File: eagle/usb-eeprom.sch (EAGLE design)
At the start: 3 parts

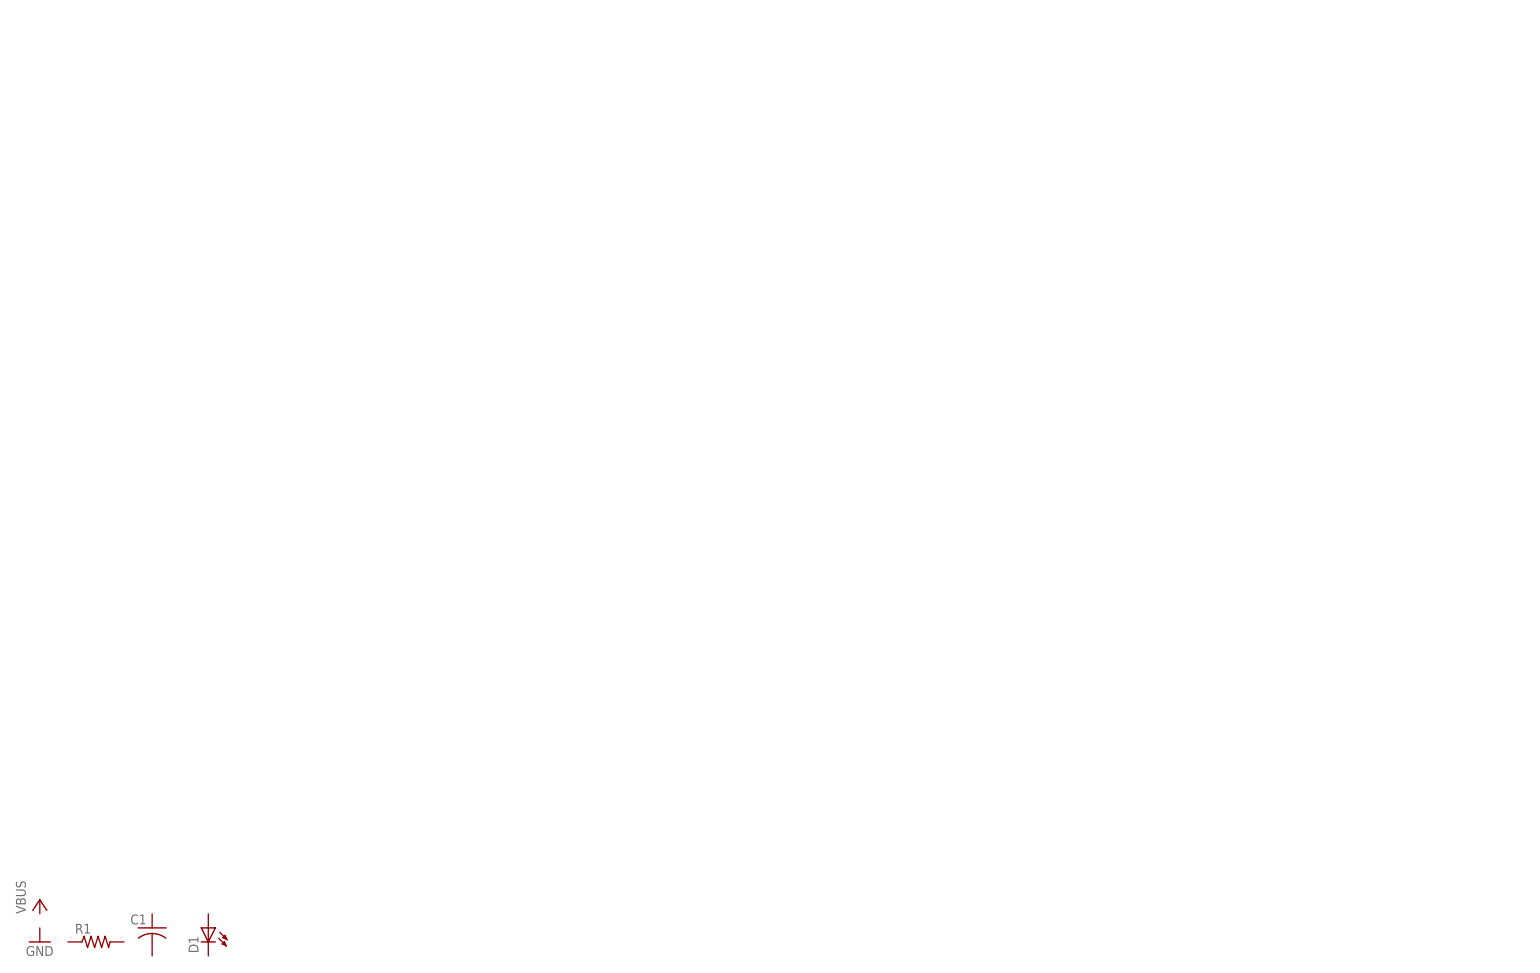
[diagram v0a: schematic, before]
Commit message: Update schematic; generate BOM
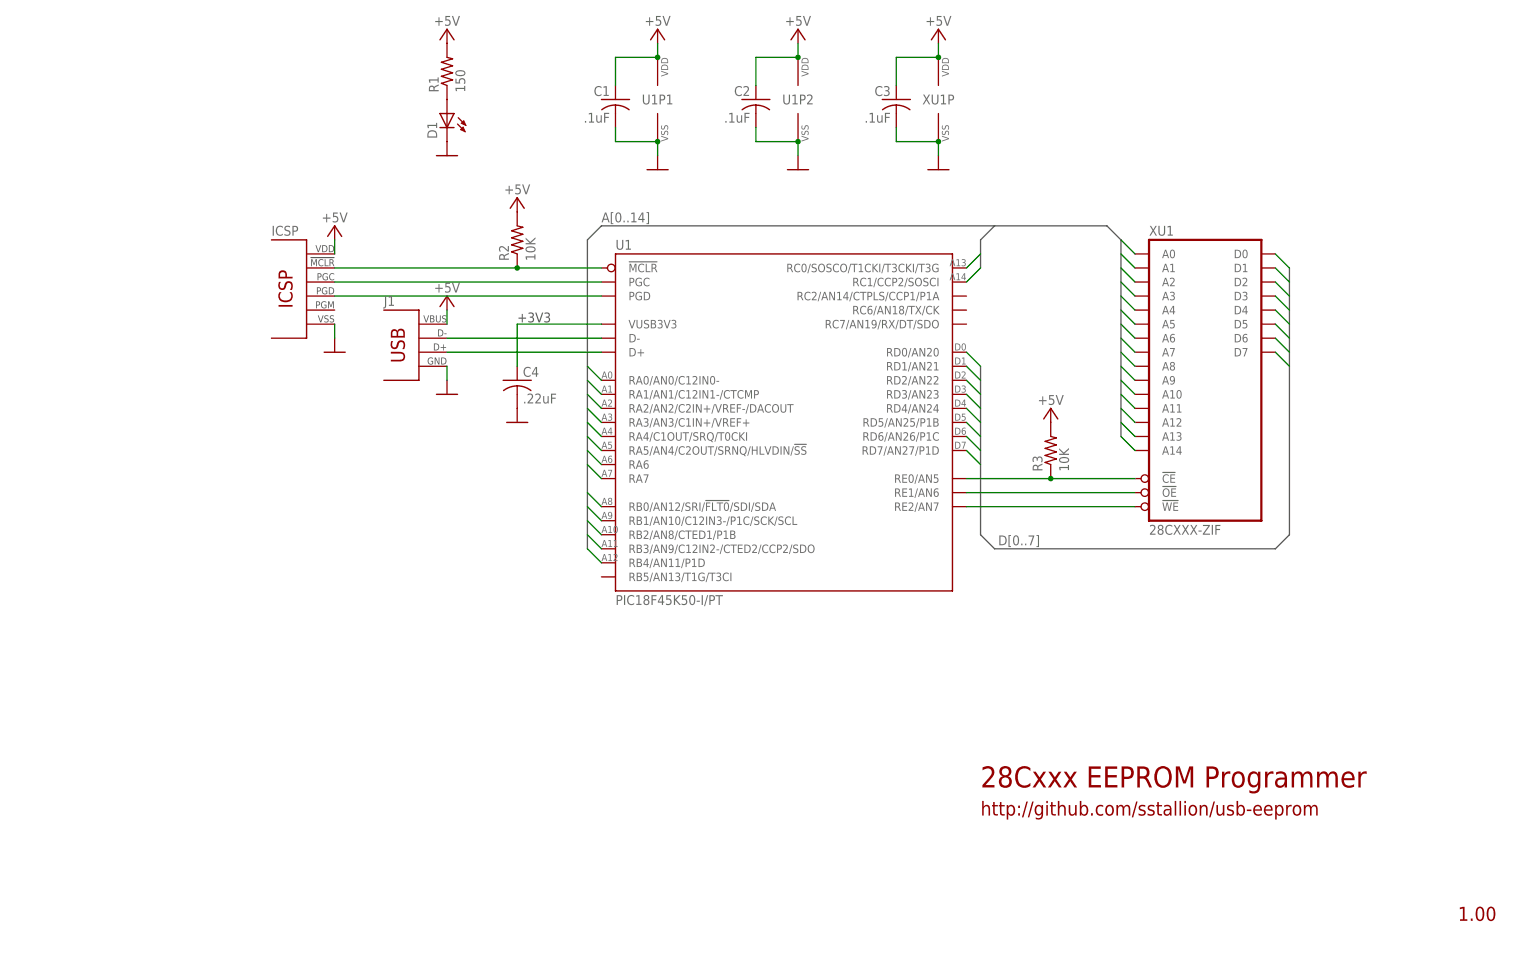
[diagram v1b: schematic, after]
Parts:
- added C2, C3: .1uF, rcl:C-USC0805
- added C4: .22uF, rcl:C-USC0805
- added ICSP: ICSP, usb-eeprom:ICSP
- added J1: USBA, usb-eeprom:USBA
- added R2, R3: 10K, rcl:R-US_R0805
- added U1: PIC18F45K50-I/PT, usb-eeprom:PIC18F45K50-I/PT
- added XU1: 28CXXX-ZIF, usb-eeprom:28CXXX-ZIF
- C1: value (none) -> .1uF; MFG (none) -> Vishay; MFG_PN (none) -> VJ0805Y104KXJCW1BC; MOUSER_PN (none) -> 77-VJ0805Y104KXJCBC; NOTES (none) -> X7R MLCC 10% 16V
- D1: value (none) -> GREEN; MFG (none) -> Kingbright; MFG_PN (none) -> APT2012SGC; MOUSER_PN (none) -> 604-APT2012SGC; NOTES (none) -> 2.2V 20mA; PARTNO APT2012SGC -> (none)
- R1: value (none) -> 150; MFG (none) -> Vishay; MFG_PN (none) -> CRCW0805150RFKEA; MOUSER_PN (none) -> 71-CRCW0805-150-E3; NOTES (none) -> 1/8W 1%
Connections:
- new net +5V: C1.1, C2.1, C3.1, ICSP.VDD, J1.1, R1.2, R2.2, R3.2, U1P1.VDD, U1P2.VDD, XU1P.VDD
- new net A0: U1A.RA0/AN0/C12IN0-, XU1A.A0
- new net A1: U1A.RA1/AN1/C12IN1-/CTCMP, XU1A.A1
- new net A10: U1A.RB2/AN8/CTED1/P1B, XU1A.A10
- new net A11: U1A.RB3/AN9/C12IN2-/CTED2/CCP2/SDO, XU1A.A11
- new net A12: U1A.RB4/AN11/P1D, XU1A.A12
- new net A13: U1A.RC0/SOSCO/T1CKI/T3CKI/T3G, XU1A.A13
- new net A14: U1A.RC1/CCP2/SOSCI, XU1A.A14
- new net A2: U1A.RA2/AN2/C2IN+/VREF-/DACOUT, XU1A.A2
- new net A3: U1A.RA3/AN3/C1IN+/VREF+, XU1A.A3
- new net A4: U1A.RA4/C1OUT/SRQ/T0CKI, XU1A.A4
- new net A5: U1A.RA5/AN4/C2OUT/SRNQ/HLVDIN/!SS!, XU1A.A5
- new net A6: U1A.RA6, XU1A.A6
- new net A7: U1A.RA7, XU1A.A7
- new net A8: U1A.RB0/AN12/SRI/!FLT0!/SDI/SDA, XU1A.A8
- new net A9: U1A.RB1/AN10/C12IN3-/P1C/SCK/SCL, XU1A.A9
- new net D0: U1A.RD0/AN20, XU1A.D0
- new net D1: U1A.RD1/AN21, XU1A.D1
- new net D2: U1A.RD2/AN22, XU1A.D2
- new net D3: U1A.RD3/AN23, XU1A.D3
- new net D4: U1A.RD4/AN24, XU1A.D4
- new net D5: U1A.RD5/AN25/P1B, XU1A.D5
- new net D6: U1A.RD6/AN26/P1C, XU1A.D6
- new net D7: U1A.RD7/AN27/P1D, XU1A.D7
- new net GND: C1.2, C2.2, C3.2, C4.2, D1.C, ICSP.VSS, J1.4, U1P1.VSS, U1P2.VSS, XU1P.VSS
- new net N$1: ICSP.!MCLR, R2.1, U1A.!MCLR
- new net N$10: D1.A, R1.1
- new net N$2: ICSP.PGC, U1A.PGC
- new net N$3: ICSP.PGD, U1A.PGD
- new net N$4: C4.1, U1A.VUSB3V3
- new net N$5: R3.1, U1A.RE0/AN5, XU1A.!CE
- new net N$6: J1.2, U1A.D-
- new net N$7: J1.3, U1A.D+
- new net N$8: U1A.RE1/AN6, XU1A.!OE
- new net N$9: U1A.RE2/AN7, XU1A.!WE
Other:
- note added: "+3V3"
- note added: "28Cxxx EEPROM Programmer"
- note added: "http://github.com/sstallion/usb-eeprom"
- moved on the sheet: C1, D1, R1

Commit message: Initial PCB layout
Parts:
- added LOGO: OSHW_LOGO_FILLX0200-NT, ohw-logo:OSHW_LOGO_FILLX0200-NT
- D1: value GREEN -> BLUE; MFG_PN APT2012SGC -> APT2012QBC/D; MOUSER_PN 604-APT2012SGC -> 604-APT2012QBC/D; NOTES 2.2V 20mA -> 3.3V 20mA
- R1: value 150 -> 100; MFG_PN CRCW0805150RFKEA -> CRCW0805100RFKEA; MOUSER_PN 71-CRCW0805-150-E3 -> 71-CRCW0805-100-E3
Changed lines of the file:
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@@
 <setting verticaltext="up"/>
 </settings>
-<grid distance="0.1" unitdist="inch" unit="inch" style="lines" multiple="1" display="yes" altdistance="0.025" altunitdist="inch" altunit="inch"/>
+<grid distance="0.1" unitdist="inch" unit="inch" style="lines" multiple="1" display="no" altdistance="0.01" altunitdist="inch" altunit="inch"/>
 <layers>
 <layer number="1" name="Top" color="4" fill="1" visible="no" active="no"/>
@@
 <attribute name="NOTES" value="1/8W 1%"/>
 </part>
-<part name="R1" library="rcl" deviceset="R-US_" device="R0805" value="150">
-<attribute name="MFG" value="Vishay"/>
-<attribute name="MFG_PN" value="CRCW0805150RFKEA"/>
-<attribute name="MOUSER_PN" value="71-CRCW0805-150-E3"/>
+<part name="R1" library="rcl" deviceset="R-US_" device="R0805" value="100">
+<attribute name="MFG" value="Vishay"/>
+<attribute name="MFG_PN" value="CRCW0805100RFKEA"/>
+<attribute name="MOUSER_PN" value="71-CRCW0805-100-E3"/>
 <attribute name="NOTES" value="1/8W 1%"/>
 </part>
-<part name="D1" library="led" deviceset="LED" device="CHIPLED_0805" value="GREEN">
+<part name="D1" library="led" deviceset="LED" device="CHIPLED_0805" value="BLUE">
 <attribute name="MFG" value="Kingbright"/>
-<attribute name="MFG_PN" value="APT2012SGC"/>
-<attribute name="MOUSER_PN" value="604-APT2012SGC"/>
-<attribute name="NOTES" value="2.2V 20mA"/>
+<attribute name="MFG_PN" value="APT2012QBC/D"/>
+<attribute name="MOUSER_PN" value="604-APT2012QBC/D"/>
+<attribute name="NOTES" value="3.3V 20mA"/>
 </part>
 <part name="C1" library="rcl" deviceset="C-US" device="C0805" value=".1uF">
@@
 <part name="P+7" library="supply1" deviceset="+5V" device=""/>
 <part name="P+8" library="supply1" deviceset="+5V" device=""/>
+<part name="LOGO" library="ohw-logo" deviceset="OSHW_LOGO_FILL" device="X0200-NT"/>
 </parts>
 <sheets>
@@
 <attribute name="VALUE" x="167.64" y="168.275" size="1.778" layer="96" align="bottom-center"/>
 </instance>
+<instance part="LOGO" gate="G$1" x="266.7" y="29.21"/>
 </instances>
 <busses>

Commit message: Replace D1 with SML0805 package
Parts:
- D1: device led:LEDCHIPLED_0805 -> led:LEDSML0805
- ICSP: MFG N/A -> (none); MFG_PN N/A -> (none); MOUSER_PN N/A -> (none); NOTES N/A -> (none)
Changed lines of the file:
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@@
 <attribute name="NOTES" value="28 PIN ZIF SOCKET"/>
 </part>
-<part name="ICSP" library="usb-eeprom" deviceset="ICSP" device="">
-<attribute name="MFG" value="N/A"/>
-<attribute name="MFG_PN" value="N/A"/>
-<attribute name="MOUSER_PN" value="N/A"/>
-<attribute name="NOTES" value="N/A"/>
-</part>
+<part name="ICSP" library="usb-eeprom" deviceset="ICSP" device=""/>
 <part name="J1" library="usb-eeprom" deviceset="USB" device="A">
 <attribute name="MFG" value="Molex"/>
@@
 <attribute name="NOTES" value="1/8W 1%"/>
 </part>
-<part name="D1" library="led" deviceset="LED" device="CHIPLED_0805" value="BLUE">
+<part name="D1" library="led" deviceset="LED" device="SML0805" value="BLUE">
 <attribute name="MFG" value="Kingbright"/>
 <attribute name="MFG_PN" value="APT2012QBC/D"/>
@@
 <attribute name="NOTES" x="215.9" y="104.14" size="1.778" layer="96" display="off"/>
 </instance>
-<instance part="ICSP" gate="G$1" x="48.26" y="119.38">
-<attribute name="MFG" x="48.26" y="119.38" size="1.778" layer="96" display="off"/>
-<attribute name="MFG_PN" x="48.26" y="119.38" size="1.778" layer="96" display="off"/>
-<attribute name="MOUSER_PN" x="48.26" y="119.38" size="1.778" layer="96" display="off"/>
-<attribute name="NOTES" x="48.26" y="119.38" size="1.778" layer="96" display="off"/>
-</instance>
+<instance part="ICSP" gate="G$1" x="48.26" y="119.38"/>
 <instance part="J1" gate="G$1" x="71.12" y="111.76">
 <attribute name="MFG" x="71.12" y="111.76" size="1.778" layer="96" display="off"/>

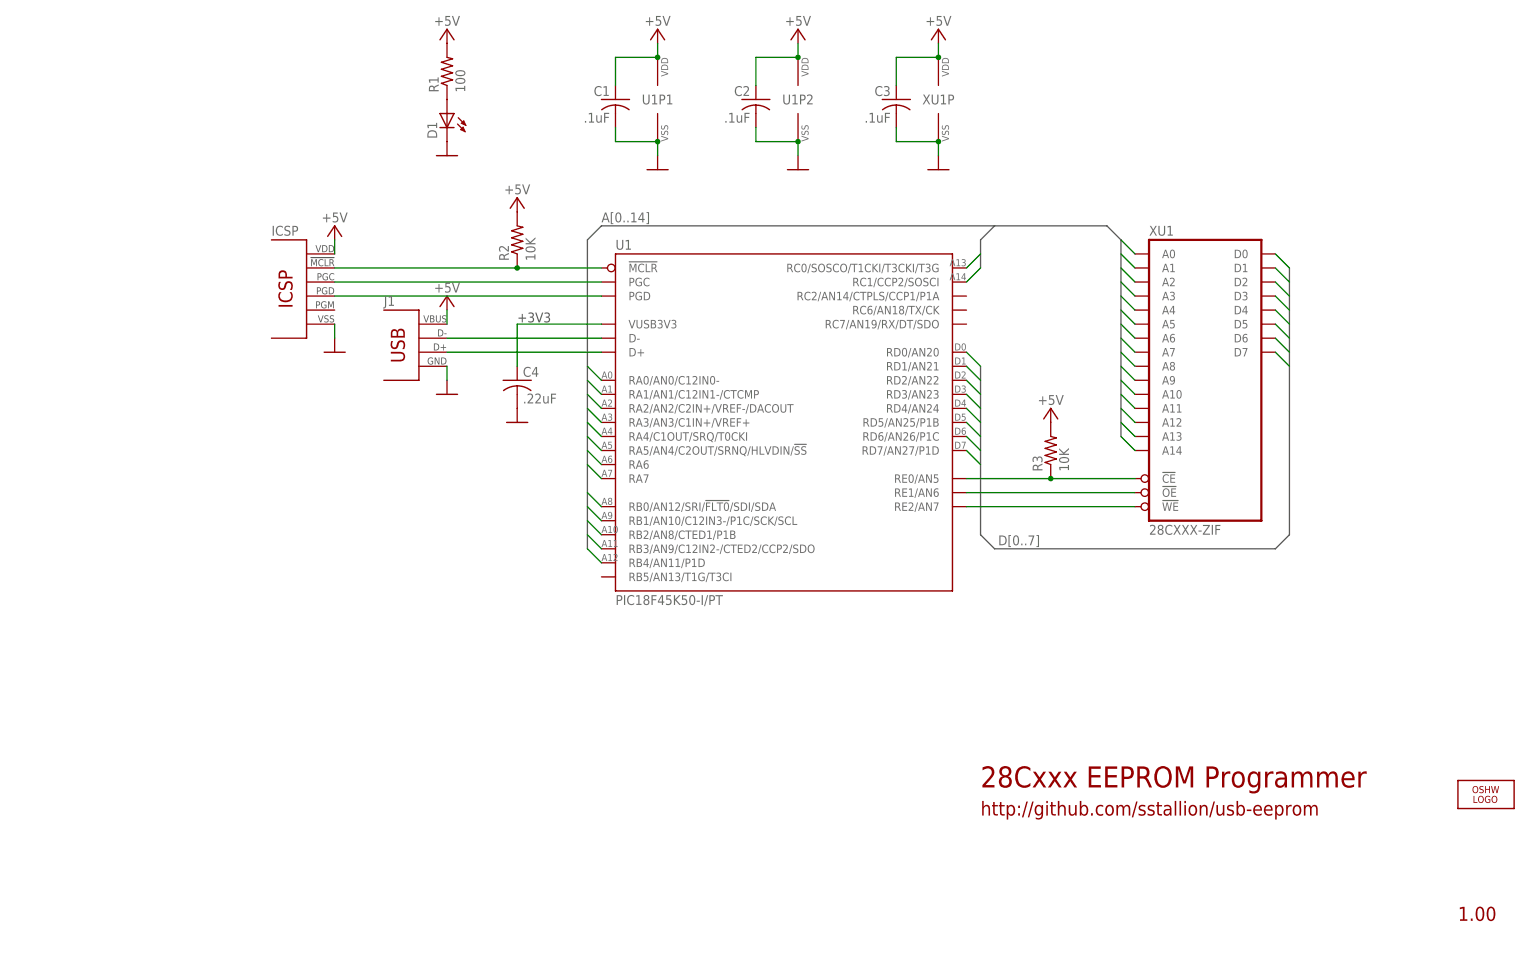
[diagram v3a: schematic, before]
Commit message: Cosmetic fixes; REV 1.01 layout
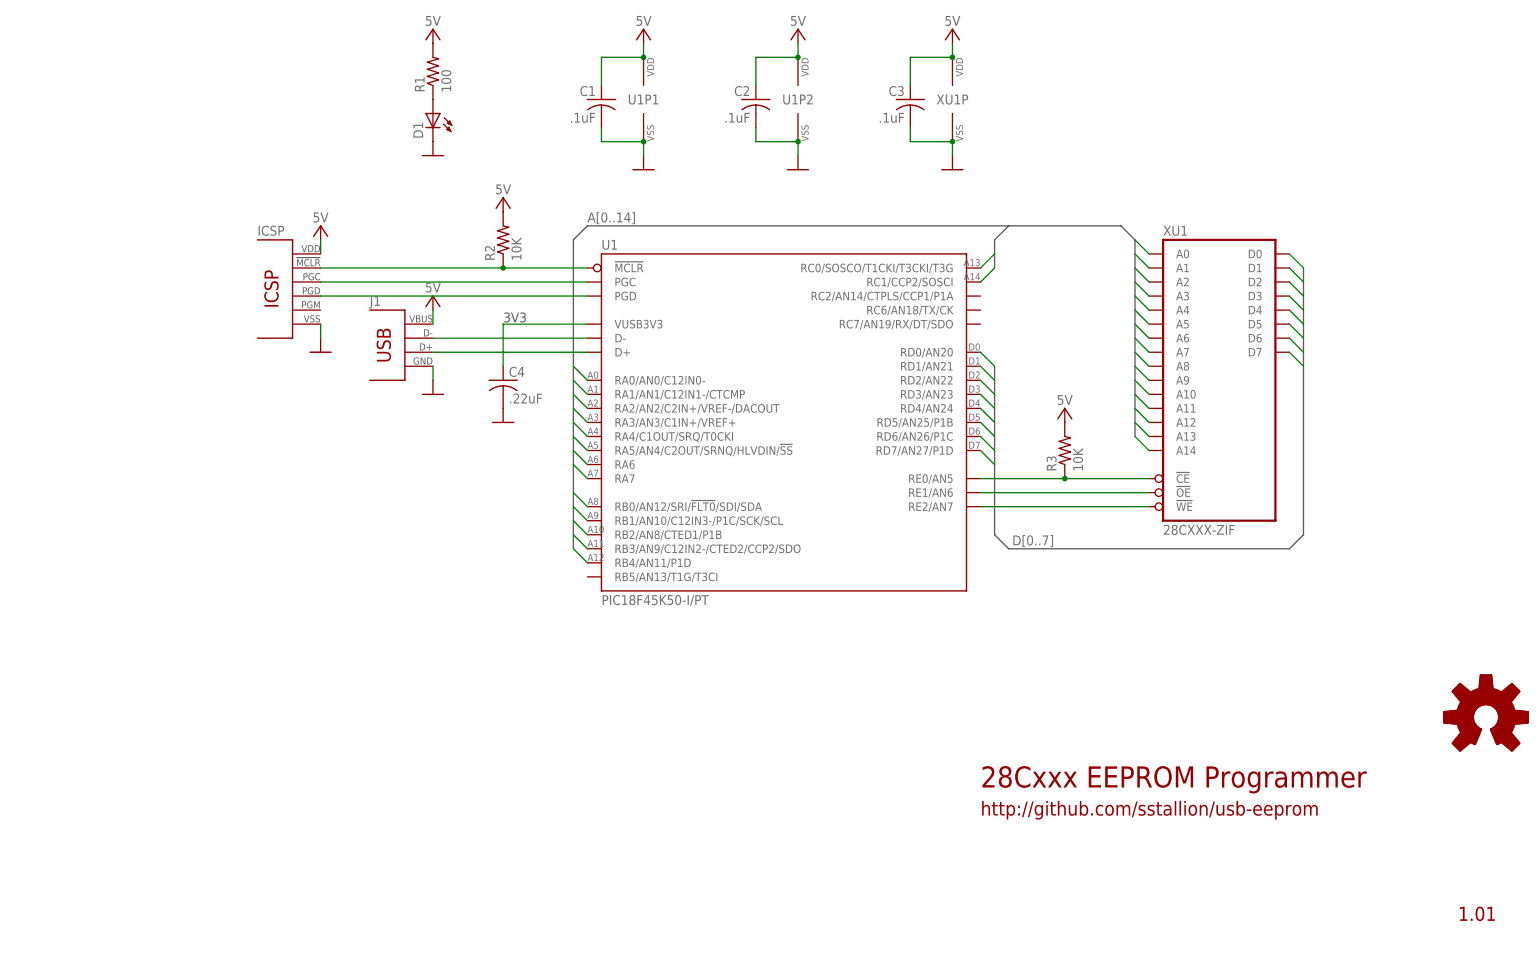
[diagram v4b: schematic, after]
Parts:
- removed LOGO: OSHW_LOGO_FILLX0200-NT, ohw-logo:OSHW_LOGO_FILLX0200-NT
- added U$1: OSHW, usb-eeprom:OSHW
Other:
- note added: "3V3"
- note removed: "+3V3"
- moved on the sheet: C1, C3, C4, D1, ICSP, J1, R1, R2, R3, U1P1, XU1, XU1P

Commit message: Update documentation
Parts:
- U1: NOTES 48MHz 32KB FLASH/RAM -> 48MHz 32KB FLASH 2KB RAM
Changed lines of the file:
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@@
 <setting verticaltext="up"/>
 </settings>
-<grid distance="0.1" unitdist="inch" unit="inch" style="lines" multiple="1" display="yes" altdistance="0.01" altunitdist="inch" altunit="inch"/>
+<grid distance="0.1" unitdist="inch" unit="inch" style="lines" multiple="1" display="no" altdistance="0.01" altunitdist="inch" altunit="inch"/>
 <layers>
 <layer number="1" name="Top" color="4" fill="1" visible="no" active="no"/>
@@
 <attribute name="MFG_PN" value="PIC18F45K50-I/PT"/>
 <attribute name="MOUSER_PN" value="579-PIC18F45K50-I/PT"/>
-<attribute name="NOTES" value="48MHz 32KB FLASH/RAM"/>
+<attribute name="NOTES" value="48MHz 32KB FLASH 2KB RAM"/>
 </part>
 <part name="R2" library="rcl" deviceset="R-US_" device="R0805" value="10K">

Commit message: Upgrade to EAGLE v6.6; update formatting
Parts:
- removed U$1: OSHW, usb-eeprom:OSHW
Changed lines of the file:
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@@
 <?xml version="1.0" encoding="utf-8"?>
 <!DOCTYPE eagle SYSTEM "eagle.dtd">
-<eagle version="6.5.0">
+<eagle version="6.6.0">
 <drawing>
 <settings>
@@
 <part name="P+7" library="supply1" deviceset="+5V" device="" value="5V"/>
 <part name="P+8" library="supply1" deviceset="+5V" device="" value="5V"/>
-<part name="U$1" library="usb-eeprom" deviceset="OSHW" device=""/>
 </parts>
 <sheets>
@@
 </plain>
 <instances>
-<instance part="FRAME1" gate="G$1" x="0" y="0" smashed="yes"/>
+<instance part="FRAME1" gate="G$1" x="0" y="0"/>
 <instance part="FRAME1" gate="G$2" x="172.72" y="0"/>
 <instance part="XU1" gate="A" x="218.44" y="104.14">
@@
 <attribute name="VALUE" x="170.18" y="168.275" size="1.778" layer="96" align="bottom-center"/>
 </instance>
-<instance part="U$1" gate="G$1" x="266.7" y="43.18"/>
 </instances>
 <busses>
